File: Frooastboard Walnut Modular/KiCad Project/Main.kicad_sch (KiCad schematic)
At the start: 251 parts, among them J10 F Row CS, J11 F Row SW, J15 F Row, J16 F Row USB, J17 Numpad, J8 Numpad CS, J9 Numpad SW, M2 Frooastboard_MM2040

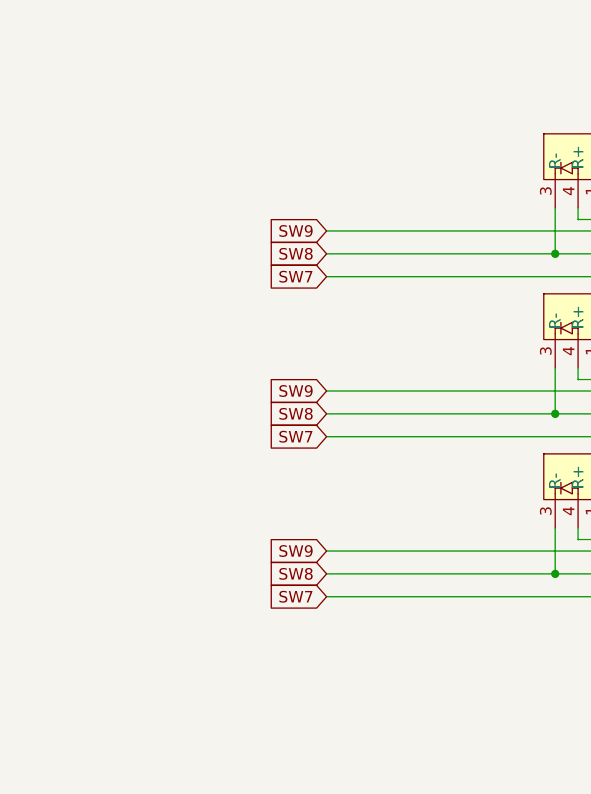
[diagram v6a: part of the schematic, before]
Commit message: add AFA01-SXXFCX-00 lib
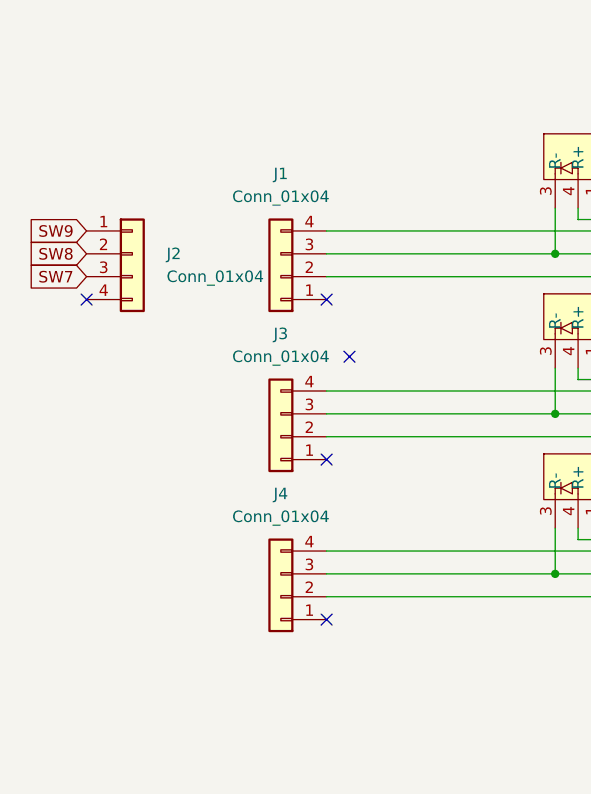
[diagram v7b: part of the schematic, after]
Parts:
- added J1, J2, J3, J4: Conn_01x04, symbol Connector_Generic:Conn_01x04
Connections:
- net SW7: now also J2.3 (Pin_3); no longer D1.1 (G-), D102.1 (G-), D110.1 (G-), D119.1 (G-), D136.1 (G-), D149.1 (G-), D162.1 (G-), D180.1 (G-), D2.1 (G-), D64.1 (G-), D68.1 (G-), D70.1 (G-), D84.1 (G-), D85.1 (G-), D86.1 (G-), D90.1 (G-), D94.1 (G-), D98.1 (G-)
- net SW8: now also J2.2 (Pin_2); no longer D1.3 (R-), D102.3 (R-), D110.3 (R-), D119.3 (R-), D136.3 (R-), D149.3 (R-), D162.3 (R-), D180.3 (R-), D2.3 (R-), D64.3 (R-), D68.3 (R-), D70.3 (R-), D84.3 (R-), D85.3 (R-), D86.3 (R-), D90.3 (R-), D94.3 (R-), D98.3 (R-)
- net SW9: now also J2.1 (Pin_1); no longer D1.5 (B-), D102.5 (B-), D110.5 (B-), D119.5 (B-), D136.5 (B-), D149.5 (B-), D162.5 (B-), D180.5 (B-), D2.5 (B-), D64.5 (B-), D68.5 (B-), D70.5 (B-), D84.5 (B-), D85.5 (B-), D86.5 (B-), D90.5 (B-), D94.5 (B-), D98.5 (B-)
- new net: D1.1 (G-), D2.1 (G-), D64.1 (G-), D68.1 (G-), D84.1 (G-), D85.1 (G-), J4.2 (Pin_2)
- new net: D1.3 (R-), D2.3 (R-), D64.3 (R-), D68.3 (R-), D84.3 (R-), D85.3 (R-), J4.3 (Pin_3)
- new net: D1.5 (B-), D2.5 (B-), D64.5 (B-), D68.5 (B-), D84.5 (B-), D85.5 (B-), J4.4 (Pin_4)
- new net: D110.1 (G-), D119.1 (G-), D136.1 (G-), D149.1 (G-), D162.1 (G-), D180.1 (G-), J1.2 (Pin_2)
- new net: D110.3 (R-), D119.3 (R-), D136.3 (R-), D149.3 (R-), D162.3 (R-), D180.3 (R-), J1.3 (Pin_3)
- new net: D110.5 (B-), D119.5 (B-), D136.5 (B-), D149.5 (B-), D162.5 (B-), D180.5 (B-), J1.4 (Pin_4)
- new net: D102.1 (G-), D70.1 (G-), D86.1 (G-), D90.1 (G-), D94.1 (G-), D98.1 (G-), J3.2 (Pin_2)
- new net: D102.3 (R-), D70.3 (R-), D86.3 (R-), D90.3 (R-), D94.3 (R-), D98.3 (R-), J3.3 (Pin_3)
- new net: D102.5 (B-), D70.5 (B-), D86.5 (B-), D90.5 (B-), D94.5 (B-), D98.5 (B-), J3.4 (Pin_4)
- no-connect marks 4 -> 9
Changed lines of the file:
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@@
   (junction (at -96.52 99.06) (diameter 0) (color 0 0 0 0)
   )
+  (no_connect (at -207.01 107.95))
+  (no_connect (at -180.34 107.95))
   (no_connect (at 320.04 165.1))
   (no_connect (at 265.43 156.21))
   (no_connect (at 320.04 167.64))
+  (no_connect (at -177.8 114.3))
+  (no_connect (at -180.34 125.73))
+  (no_connect (at -180.34 143.51))
   (no_connect (at 265.43 140.97))
   (wire (pts (xy 154.94 71.12) (xy 154.94 72.39))
@@
     )
   )
-  (global_label "SW9" (shape input) (at -180.34 135.89 180) (fields_autoplaced)
-    (effects (font (size 1.27 1.27)) (justify right))
-    (property "Intersheetrefs" "${INTERSHEET_REFS}" (at -186.6236 135.9694 0)
-      (effects (font (size 1.27 1.27)) (justify right) hide)
-    )
-  )
   (global_label "CS9" (shape input) (at 270.51 223.52 180) (fields_autoplaced)
     (effects (font (size 1.27 1.27)) (justify right))
@@
     )
   )
-  (global_label "SW9" (shape input) (at -180.34 100.33 180) (fields_autoplaced)
+  (global_label "SW9" (shape input) (at -207.01 100.33 180) (fields_autoplaced)
     (effects (font (size 1.27 1.27)) (justify right))
-    (property "Intersheetrefs" "${INTERSHEET_REFS}" (at -186.6236 100.4094 0)
+    (property "Intersheetrefs" "${INTERSHEET_REFS}" (at -213.2936 100.4094 0)
       (effects (font (size 1.27 1.27)) (justify right) hide)
     )
@@
     )
   )
-  (global_label "SW8" (shape input) (at -180.34 120.65 180) (fields_autoplaced)
-    (effects (font (size 1.27 1.27)) (justify right))
-    (property "Intersheetrefs" "${INTERSHEET_REFS}" (at -186.6236 120.7294 0)
-      (effects (font (size 1.27 1.27)) (justify right) hide)
-    )
-  )
   (global_label "CS12" (shape input) (at 297.18 26.67 90) (fields_autoplaced)
     (effects (font (size 1.27 1.27)) (justify left))
@@
     )
   )
-  (global_label "SW8" (shape input) (at -180.34 138.43 180) (fields_autoplaced)
-    (effects (font (size 1.27 1.27)) (justify right))
-    (property "Intersheetrefs" "${INTERSHEET_REFS}" (at -186.6236 138.5094 0)
-      (effects (font (size 1.27 1.27)) (justify right) hide)
-    )
-  )
   (global_label "CS4" (shape input) (at 241.3 209.55 180) (fields_autoplaced)
     (effects (font (size 1.27 1.27)) (justify right))
@@
     )
   )
-  (global_label "SW9" (shape input) (at -180.34 118.11 180) (fields_autoplaced)
-    (effects (font (size 1.27 1.27)) (justify right))
-    (property "Intersheetrefs" "${INTERSHEET_REFS}" (at -186.6236 118.1894 0)
-      (effects (font (size 1.27 1.27)) (justify right) hide)
-    )
-  )
   (global_label "CS2" (shape input) (at 344.17 125.73 90) (fields_autoplaced)
     (effects (font (size 1.27 1.27)) (justify left))
@@
     )
   )
-  (global_label "SW7" (shape input) (at -180.34 140.97 180) (fields_autoplaced)
-    (effects (font (size 1.27 1.27)) (justify right))
-    (property "Intersheetrefs" "${INTERSHEET_REFS}" (at -186.6236 141.0494 0)
-      (effects (font (size 1.27 1.27)) (justify right) hide)
-    )
-  )
   (global_label "SW2" (shape input) (at 270.51 248.92 180) (fields_autoplaced)
     (effects (font (size 1.27 1.27)) (justify right))
@@
     )
   )
-  (global_label "SW7" (shape input) (at -180.34 105.41 180) (fields_autoplaced)
+  (global_label "SW7" (shape input) (at -207.01 105.41 180) (fields_autoplaced)
     (effects (font (size 1.27 1.27)) (justify right))
-    (property "Intersheetrefs" "${INTERSHEET_REFS}" (at -186.6236 105.4894 0)
+    (property "Intersheetrefs" "${INTERSHEET_REFS}" (at -213.2936 105.4894 0)
       (effects (font (size 1.27 1.27)) (justify right) hide)
     )
@@
     )
   )
-  (global_label "SW7" (shape input) (at -180.34 123.19 180) (fields_autoplaced)
-    (effects (font (size 1.27 1.27)) (justify right))
-    (property "Intersheetrefs" "${INTERSHEET_REFS}" (at -186.6236 123.2694 0)
-      (effects (font (size 1.27 1.27)) (justify right) hide)
-    )
-  )
   (global_label "CS15" (shape input) (at 317.5 152.4 180) (fields_autoplaced)
     (effects (font (size 1.27 1.27)) (justify right))
@@
     )
   )
-  (global_label "SW8" (shape input) (at -180.34 102.87 180) (fields_autoplaced)
+  (global_label "SW8" (shape input) (at -207.01 102.87 180) (fields_autoplaced)
     (effects (font (size 1.27 1.27)) (justify right))
-    (property "Intersheetrefs" "${INTERSHEET_REFS}" (at -186.6236 102.9494 0)
+    (property "Intersheetrefs" "${INTERSHEET_REFS}" (at -213.2936 102.9494 0)
       (effects (font (size 1.27 1.27)) (justify right) hide)
     )
@@
     )
   )
+  (symbol (lib_id "Connector_Generic:Conn_01x04") (at -185.42 123.19 180) (unit 1)
+    (in_bom yes) (on_board yes) (dnp no) (fields_autoplaced)
+    (property "Reference" "J3" (at -185.42 111.76 0)
+      (effects (font (size 1.27 1.27)))
+    )
+    (property "Value" "Conn_01x04" (at -185.42 114.3 0)
+      (effects (font (size 1.27 1.27)))
+    )
+    (property "Footprint" "" (at -185.42 123.19 0)
+      (effects (font (size 1.27 1.27)) hide)
+    )
+    (property "Datasheet" "~" (at -185.42 123.19 0)
+      (effects (font (size 1.27 1.27)) hide)
+    )
+    (pin "1")
+    (pin "2")
+    (pin "3")
+    (pin "4")
+    (instances
+      (project "Frooastboard Walnut Modular"
+        (path "/e63e39d7-6ac0-4ffd-8aa3-1841a4541b55/da496a6d-9c73-4726-8a69-2d6a4df38c58"
+          (reference "J3") (unit 1)
+        )
+      )
+    )
+  )
   (symbol (lib_id "MX_Alps_Hybrid:MX-NoLED") (at 193.04 236.22 0) (unit 1)
     (in_bom yes) (on_board yes) (dnp no) (fields_autoplaced)
@@
     )
   )
+  (symbol (lib_id "Connector_Generic:Conn_01x04") (at -185.42 105.41 180) (unit 1)
+    (in_bom yes) (on_board yes) (dnp no) (fields_autoplaced)
+    (property "Reference" "J1" (at -185.42 93.98 0)
+      (effects (font (size 1.27 1.27)))
+    )
+    (property "Value" "Conn_01x04" (at -185.42 96.52 0)
+      (effects (font (size 1.27 1.27)))
+    )
+    (property "Footprint" "" (at -185.42 105.41 0)
+      (effects (font (size 1.27 1.27)) hide)
+    )
+    (property "Datasheet" "~" (at -185.42 105.41 0)
+      (effects (font (size 1.27 1.27)) hide)
+    )
+    (pin "1")
+    (pin "2")
+    (pin "3")
+    (pin "4")
+    (instances
+      (project "Frooastboard Walnut Modular"
+        (path "/e63e39d7-6ac0-4ffd-8aa3-1841a4541b55/da496a6d-9c73-4726-8a69-2d6a4df38c58"
+          (reference "J1") (unit 1)
+        )
+      )
+    )
+  )
   (symbol (lib_id "MX_Alps_Hybrid:MX-NoLED") (at 128.27 234.95 0) (unit 1)
     (in_bom yes) (on_board yes) (dnp no) (fields_autoplaced)
@@
     )
   )
+  (symbol (lib_id "Connector_Generic:Conn_01x04") (at -185.42 140.97 180) (unit 1)
+    (in_bom yes) (on_board yes) (dnp no) (fields_autoplaced)
+    (property "Reference" "J4" (at -185.42 129.54 0)
+      (effects (font (size 1.27 1.27)))
+    )
+    (property "Value" "Conn_01x04" (at -185.42 132.08 0)
+      (effects (font (size 1.27 1.27)))
+    )
+    (property "Footprint" "" (at -185.42 140.97 0)
+      (effects (font (size 1.27 1.27)) hide)
+    )
+    (property "Datasheet" "~" (at -185.42 140.97 0)
+      (effects (font (size 1.27 1.27)) hide)
+    )
+    (pin "1")
+    (pin "2")
+    (pin "3")
+    (pin "4")
+    (instances
+      (project "Frooastboard Walnut Modular"
+        (path "/e63e39d7-6ac0-4ffd-8aa3-1841a4541b55/da496a6d-9c73-4726-8a69-2d6a4df38c58"
+          (reference "J4") (unit 1)
+        )
+      )
+    )
+  )
   (symbol (lib_id "Frooastboard Symbols:RGB_LED_6_Pin") (at -102.87 90.17 0) (unit 1)
     (in_bom yes) (on_board yes) (dnp no) (fields_autoplaced)
@@
         )
       )
+    )
+  )
+  (symbol (lib_id "Connector_Generic:Conn_01x04") (at -201.93 102.87 0) (unit 1)
+    (in_bom yes) (on_board yes) (dnp no) (fields_autoplaced)
+    (property "Reference" "J2" (at -198.12 102.87 0)
+      (effects (font (size 1.27 1.27)) (justify left))
+    )
+    (property "Value" "Conn_01x04" (at -198.12 105.41 0)
+      (effects (font (size 1.27 1.27)) (justify left))
+    )
+    (property "Footprint" "" (at -201.93 102.87 0)
+      (effects (font (size 1.27 1.27)) hide)
+    )
+    (property "Datasheet" "~" (at -201.93 102.87 0)
+      (effects (font (size 1.27 1.27)) hide)
+    )
+    (pin "1")
+    (pin "2")
+    (pin "3")
+    (pin "4")
+    (instances
+      (project "Frooastboard Walnut Modular"
+        (path "/e63e39d7-6ac0-4ffd-8aa3-1841a4541b55/da496a6d-9c73-4726-8a69-2d6a4df38c58"
+          (reference "J2") (unit 1)
+        )
+      )

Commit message: fix symbols and remove lck
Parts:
- removed J1, J2, J3, J4: Conn_01x04, symbol Connector_Generic:Conn_01x04
- removed J10: F Row CS, Connector_PinHeader_1.27mm:PinHeader_1x16_P1.27mm_Vertical, symbol Connector:Conn_01x16_Socket
- removed J11: F Row SW, Connector_PinHeader_1.27mm:PinHeader_1x06_P1.27mm_Vertical, symbol Connector:Conn_01x06_Socket
- removed J15: F Row, Connector_PinHeader_1.27mm:PinHeader_1x10_P1.27mm_Vertical, symbol Connector:Conn_01x10_Socket
- removed J16: F Row USB, Connector_PinHeader_1.27mm:PinHeader_1x04_P1.27mm_Vertical, symbol Connector:Conn_01x04_Socket
- removed J17: Numpad, Connector_PinHeader_1.27mm:PinHeader_1x13_P1.27mm_Vertical, symbol Connector:Conn_01x13_Socket
- removed J8: Numpad CS, Connector_PinHeader_1.27mm:PinHeader_1x16_P1.27mm_Vertical, symbol Connector:Conn_01x15_Socket
- removed J9: Numpad SW, Connector_PinHeader_1.27mm:PinHeader_1x06_P1.27mm_Vertical, symbol Connector:Conn_01x06_Socket
- added FPC1, FPC2, FPC3, FPC4: AFA01-S04FCC-00, kicad_lceda:FPC-SMD_AFA01-S04FCC-00, symbol AFA01-SXXFCX-00:AFA01-S04FCC-00
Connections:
- net COL0: no longer M2.12 (COL0)
- net COL1: no longer M2.13 (COL1)
- net COL2: no longer M2.14 (COL2)
- net COL3: no longer M2.15 (COL3)
- net COL4: no longer M2.16 (COL4)
- net COL5: no longer M2.17 (COL5)
- net COL6: no longer M2.18 (COL6)
- net COL7: no longer M2.19 (COL7)
- net COL8: no longer M2.20 (COL8)
- net COL9: no longer M2.21 (COL9)
- net GND: now also FPC1.4, FPC1.5, FPC1.6, FPC2.1, FPC2.5, FPC2.6, FPC3.1, FPC3.5, FPC3.6, FPC4.1, FPC4.5, FPC4.6
- net SW7: now also FPC1.3
- net SW8: now also FPC1.2
- net SW9: now also FPC1.1
- net at D1.1 (G-), D2.1 (G-), D64.1 (G-)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: now also FPC4.2
- net at D1.3 (R-), D2.3 (R-), D64.3 (R-)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: now also FPC4.3
- net at D1.5 (B-), D2.5 (B-), D64.5 (B-)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: now also FPC4.4
- net at D110.1 (G-), D119.1 (G-), D136.1 (G-)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: now also FPC2.2
- net at D110.3 (R-), D119.3 (R-), D136.3 (R-)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: now also FPC2.3
- net at D110.5 (B-), D119.5 (B-), D136.5 (B-)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: now also FPC2.4
- net at D102.1 (G-), D70.1 (G-), D86.1 (G-)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: now also FPC3.2
- net at D102.3 (R-), D70.3 (R-), D86.3 (R-)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: now also FPC3.3
- net at D102.5 (B-), D70.5 (B-), D86.5 (B-)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: now also FPC3.4
- new net ce_col0: M2.12 (COL0)
- new net ce_col1: M2.13 (COL1)
- new net ce_col2: M2.14 (COL2)
- new net ce_col3: M2.15 (COL3)
- new net ce_col4: M2.16 (COL4)
- new net ce_col5: M2.17 (COL5)
- new net ce_col6: M2.18 (COL6)
- new net ce_col7: M2.19 (COL7)
- new net ce_col8: M2.20 (COL8)
- new net ce_col9: M2.21 (COL9)
- no-connect marks 9 -> 4
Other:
- moved on the sheet: D1, D102, D2, D64, D68, D70, D84, D85, D86, D90, D94, D98
